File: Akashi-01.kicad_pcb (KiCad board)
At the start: 2 copper layers, 71.1 x 67.3 mm, 33 parts, among them CN10 PPPC192LFBN-RC, CN7 PPPC192LFBN-RC, SW1 PEC11R-4220F-S0024

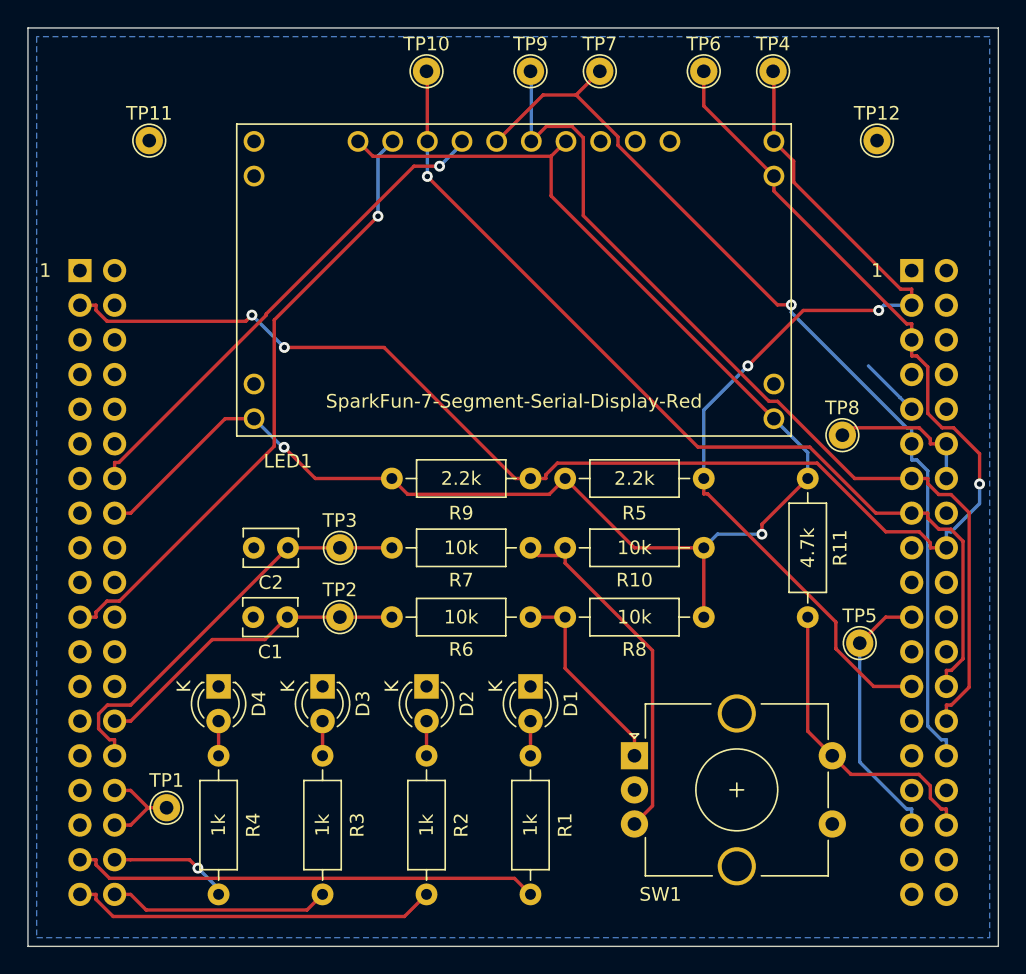
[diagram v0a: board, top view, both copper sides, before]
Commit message: Serial LED has been fixed.
Issue : Serial 7 segment module has wrong pin assigment. #3
https://github.com/suikan4github/Suikan-KiCad-Libraries/issues/3
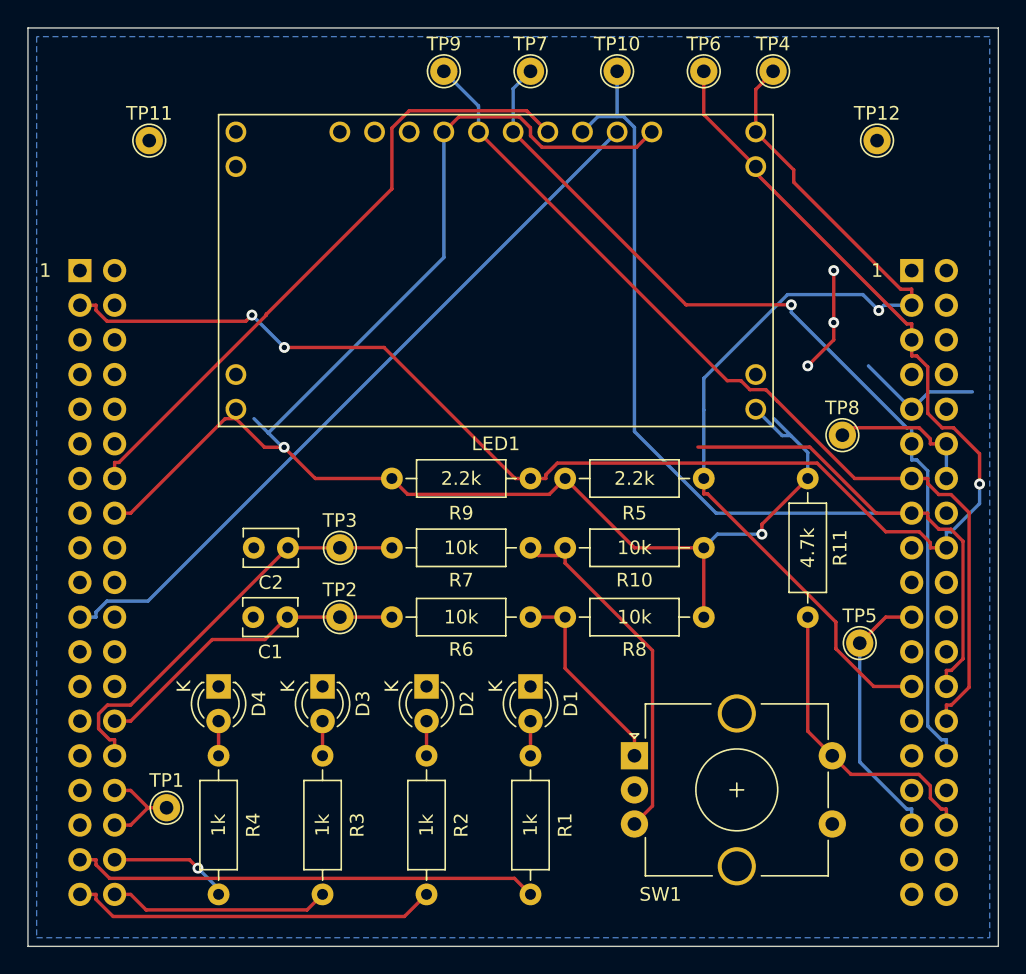
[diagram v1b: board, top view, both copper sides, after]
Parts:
- moved TP10 14.0 mm to (158.8, 46.4)
- moved TP9 6.35 mm to (146.1, 46.4)
- moved TP7 5.08 mm to (152.4, 46.4)
- moved LED1 1.50 mm to (130.8, 50.8)
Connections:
- LED1 pad 10: GND -> /nLEDCS
- LED1 pad 11: GND -> /SPI1_MOSI
- LED1 pad 12: +3V3 -> /nRESET
- LED1 pad 13: /SPI1_MISO -> /SPI1_SCK
- LED1 pad 14: /SPI1_SCK -> /SPI1_MISO
- LED1 pad 15: /nRESET -> +3V3
- LED1 pad 16: /SPI1_MOSI -> GND
- LED1 pad 17: /nLEDCS -> GND
- LED1 pad 18: +3V3 -> GND
- LED1 pad 9: GND -> +3V3
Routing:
- net /SPI1_MOSI: track 69.6 -> 86.9 mm, vias 1 -> 0
- net GND: track 4.49 -> 17.2 mm, vias 0 -> 3
- net /nRESET: track 36.5 -> 46.9 mm, vias 1 -> 0
- net +3V3: track 113.7 -> 123.5 mm
- net /nLEDCS: track 45.6 -> 54.3 mm, vias 1 -> 0
- net /I2C1_SCL: track 68.6 -> 72.1 mm, vias 2 -> 1
- net /SPI1_SCK: track 70.6 -> 69.0 mm
- net /UART1_TX: track 19.1 -> 19.7 mm
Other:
- board text added: "Akashi-01 v1.0.2 A Murasaki JIG for Nucleo 64 (C) Seiichi Horie 2019 https://github.com/suikan4github/Akashi-01"
- board text removed: "Akashi-01 v1.0.1 A Murasaki JIG for Nucleo 64 (C) Seiichi Horie 2019 https://github.com/suikan4github/Akashi-01"

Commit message: Modify the mistaken connection of SCL/SDA to LED module.
LED1 module SCL/SDA is connected reverse. #7
https://github.com/suikan4github/Akashi-01/issues/7
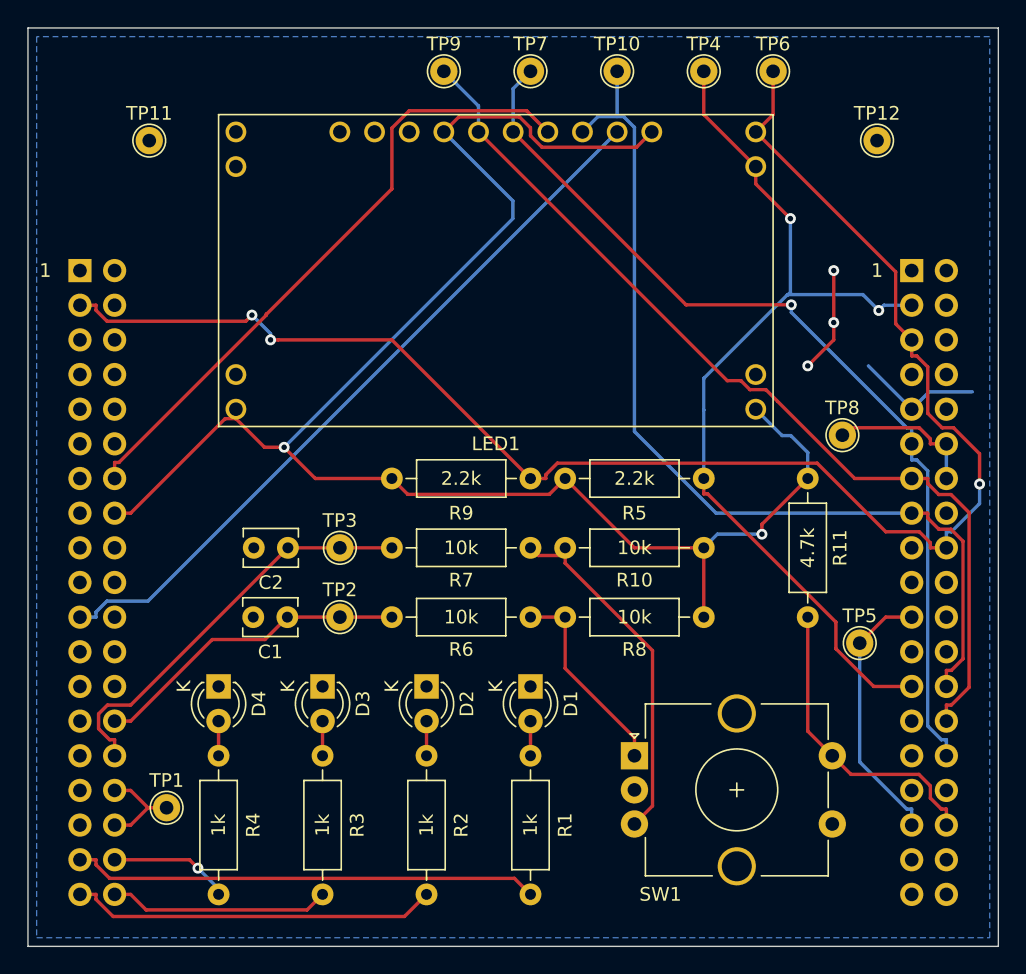
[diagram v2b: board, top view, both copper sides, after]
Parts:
- moved TP4 5.08 mm to (165.1, 46.4)
- moved TP6 5.08 mm to (170.2, 46.4)
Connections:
- CN10 pad 1: (no net) -> Net-(CN10-Pad1)
- CN10 pad 10: (no net) -> Net-(CN10-Pad10)
- CN10 pad 16: (no net) -> Net-(CN10-Pad16)
- CN10 pad 17: (no net) -> Net-(CN10-Pad17)
- CN10 pad 19: (no net) -> Net-(CN10-Pad19)
- CN10 pad 2: (no net) -> Net-(CN10-Pad2)
- CN10 pad 22: (no net) -> Net-(CN10-Pad22)
- CN10 pad 23: (no net) -> Net-(CN10-Pad23)
- CN10 pad 24: (no net) -> Net-(CN10-Pad24)
- CN10 pad 27: (no net) -> Net-(CN10-Pad27)
- CN10 pad 29: (no net) -> Net-(CN10-Pad29)
- CN10 pad 31: (no net) -> Net-(CN10-Pad31)
- CN10 pad 32: (no net) -> Net-(CN10-Pad32)
- CN10 pad 35: (no net) -> Net-(CN10-Pad35)
- CN10 pad 36: (no net) -> Net-(CN10-Pad36)
- CN10 pad 37: (no net) -> Net-(CN10-Pad37)
- CN10 pad 38: (no net) -> Net-(CN10-Pad38)
- CN10 pad 4: (no net) -> Net-(CN10-Pad4)
- CN10 pad 6: (no net) -> Net-(CN10-Pad6)
- CN10 pad 7: (no net) -> Net-(CN10-Pad7)
- CN10 pad 8: (no net) -> Net-(CN10-Pad8)
- CN7 pad 1: (no net) -> Net-(CN7-Pad1)
- CN7 pad 10: (no net) -> Net-(CN7-Pad10)
- CN7 pad 11: (no net) -> Net-(CN7-Pad11)
- CN7 pad 12: (no net) -> Net-(CN7-Pad12)
- CN7 pad 13: (no net) -> Net-(CN7-Pad13)
- CN7 pad 15: (no net) -> Net-(CN7-Pad15)
- CN7 pad 17: (no net) -> Net-(CN7-Pad17)
- CN7 pad 18: (no net) -> Net-(CN7-Pad18)
- CN7 pad 2: (no net) -> Net-(CN7-Pad2)
- CN7 pad 23: (no net) -> Net-(CN7-Pad23)
- CN7 pad 24: (no net) -> Net-(CN7-Pad24)
- CN7 pad 25: (no net) -> Net-(CN7-Pad25)
- CN7 pad 26: (no net) -> Net-(CN7-Pad26)
- CN7 pad 27: (no net) -> Net-(CN7-Pad27)
- CN7 pad 29: (no net) -> Net-(CN7-Pad29)
- CN7 pad 31: (no net) -> Net-(CN7-Pad31)
- CN7 pad 33: (no net) -> Net-(CN7-Pad33)
- CN7 pad 4: (no net) -> Net-(CN7-Pad4)
- CN7 pad 5: (no net) -> Net-(CN7-Pad5)
- CN7 pad 6: (no net) -> Net-(CN7-Pad6)
- CN7 pad 7: (no net) -> Net-(CN7-Pad7)
- CN7 pad 9: (no net) -> Net-(CN7-Pad9)
- LED1 pad 1: (no net) -> Net-(LED1-Pad1)
- LED1 pad 2: (no net) -> Net-(LED1-Pad2)
- LED1 pad 7: /I2C1_SDA -> /I2C1_SCL
- LED1 pad 8: /I2C1_SCL -> /I2C1_SDA
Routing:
- net /SPI1_MOSI: track 86.9 -> 69.2 mm
- net /I2C1_SCL: track 72.1 -> 68.7 mm, vias 1 -> 2
- net /I2C1_SDA: track 118.2 -> 116.9 mm
